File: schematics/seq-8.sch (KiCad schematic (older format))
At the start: 57 parts

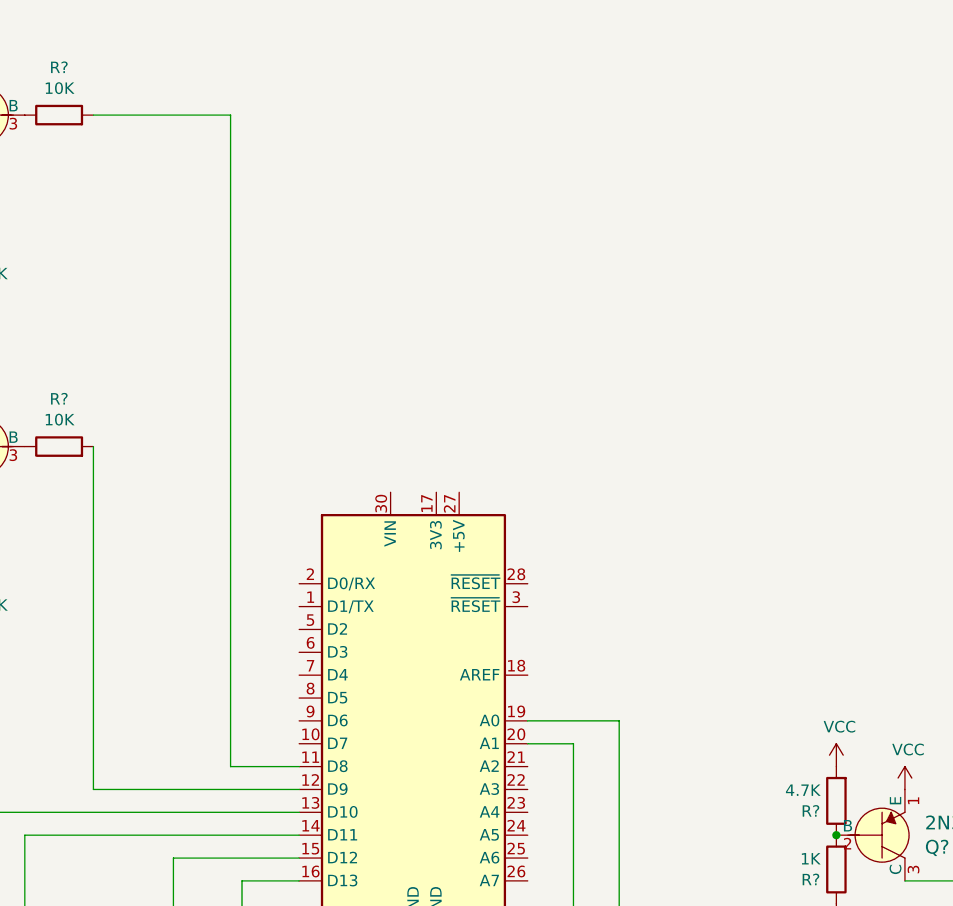
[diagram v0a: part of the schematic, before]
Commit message: add clock and reset inputs
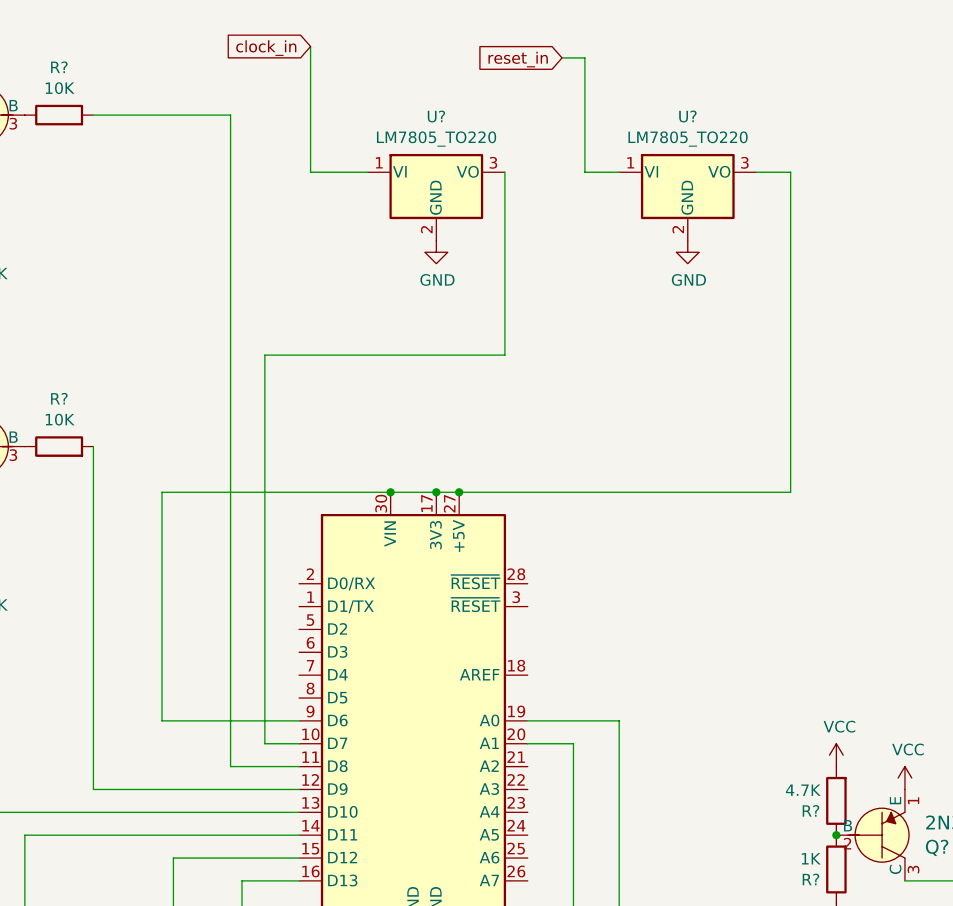
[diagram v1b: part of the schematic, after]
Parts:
- added U? (x2): LM7805_TO220, Package_TO_SOT_THT:TO-220-3_Vertical, symbol Regulator_Linear:LM7805_TO220
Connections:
- net labels added: clock_in, reset_in
- wire segments 65 -> 82
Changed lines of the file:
@@
 encoding utf-8
 Sheet 1 1
-Title ""
+Title "8 Step Sequencer"
 Date ""
 Rev ""
-Comp ""
-Comment1 ""
-Comment2 ""
+Comp "toastynerd <Tyler Morgan>"
+Comment1 "2020 Creative Commons Non Commercial"
+Comment2 "8 Step Sequencer"
 Comment3 ""
 Comment4 ""
@@
 Wire Wire Line
 	9900 10250 10800 10250
+$Comp
+L Regulator_Linear:LM7805_TO220 U?
+U 1 1 5FA26E7E
+P 9800 1400
+F 0 "U?" H 9800 1642 50  0000 C CNN
+F 1 "LM7805_TO220" H 9800 1551 50  0000 C CNN
+F 2 "Package_TO_SOT_THT:TO-220-3_Vertical" H 9800 1625 50  0001 C CIN
+F 3 "http://www.fairchildsemi.com/ds/LM/LM7805.pdf" H 9800 1350 50  0001 C CNN
+	1    9800 1400
+	1    0    0    -1
+$EndComp
+Text GLabel 9250 850  0    50   Input ~ 0
+clock_in
+Wire Wire Line
+	9500 1400 9250 1400
+Wire Wire Line
+	9250 1400 9250 850
+$Comp
+L power:GND #PWR?
+U 1 1 5FA2EA21
+P 9800 1700
+F 0 "#PWR?" H 9800 1450 50  0001 C CNN
+F 1 "GND" H 9805 1527 50  0000 C CNN
+F 2 "" H 9800 1700 50  0001 C CNN
+F 3 "" H 9800 1700 50  0001 C CNN
+	1    9800 1700
+	1    0    0    -1
+$EndComp
+Wire Wire Line
+	9200 3900 9050 3900
+Wire Wire Line
+	9050 3900 9050 2200
+Wire Wire Line
+	9050 2200 10100 2200
+Wire Wire Line
+	10100 2200 10100 1400
+$Comp
+L Regulator_Linear:LM7805_TO220 U?
+U 1 1 5FA34670
+P 10900 1400
+F 0 "U?" H 10900 1642 50  0000 C CNN
+F 1 "LM7805_TO220" H 10900 1551 50  0000 C CNN
+F 2 "Package_TO_SOT_THT:TO-220-3_Vertical" H 10900 1625 50  0001 C CIN
+F 3 "http://www.fairchildsemi.com/ds/LM/LM7805.pdf" H 10900 1350 50  0001 C CNN
+	1    10900 1400
+	1    0    0    -1
+$EndComp
+Text GLabel 10350 900  0    50   Input ~ 0
+reset_in
+Wire Wire Line
+	10350 900  10450 900
+Wire Wire Line
+	10450 900  10450 1400
+Wire Wire Line
+	10450 1400 10600 1400
+$Comp
+L power:GND #PWR?
+U 1 1 5FA3BE86
+P 10900 1700
+F 0 "#PWR?" H 10900 1450 50  0001 C CNN
+F 1 "GND" H 10905 1527 50  0000 C CNN
+F 2 "" H 10900 1700 50  0001 C CNN
+F 3 "" H 10900 1700 50  0001 C CNN
+	1    10900 1700
+	1    0    0    -1
+$EndComp
+Wire Wire Line
+	11200 1400 11350 1400
+Wire Wire Line
+	11350 1400 11350 2800
+Wire Wire Line
+	11350 2800 9900 2800
+Wire Wire Line
+	8600 2800 8600 3800
+Wire Wire Line
+	8600 3800 9200 3800
+Connection ~ 9600 2800
+Wire Wire Line
+	9600 2800 8600 2800
+Connection ~ 9800 2800
+Wire Wire Line
+	9800 2800 9600 2800
+Connection ~ 9900 2800
+Wire Wire Line
+	9900 2800 9800 2800
 $EndSCHEMATC
